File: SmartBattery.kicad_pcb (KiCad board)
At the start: 4 copper layers, 100 x 80 mm, 479 parts, among them J1 USB_C_Receptacle_USB2.0, J10 JST 2P-1.0, J11 JST 2P-1.0, J12 Conn_02x05_Odd_Even, J13 Conn_01x03_Male, J14 Conn_01x03_Male, J15 USB_C_Receptacle_USB2.0, J16 DM3AT-SF-PEJM5, J17 Conn_02x05_Odd_Even, J2 ST-USB-003A, J3 JACK-C-PC-10A-RA(R), J4 JST 2P-1.0, J5 JST 2P-1.0, J6 JST 2P-1.0, J7 JST 2P-1.0, J8 JST 2P-1.0, J9 JST 2P-1.0, Q1 VBA2625, Q10 AON7400A, Q11 AON7400A, Q12 BSC067N06LS3, Q13 BSC067N06LS3, Q14 2n7002K, Q15 VBA2625, Q16 VBA2625, Q17 VBA2625, Q18 VBA2625, Q19 VBA2625, Q2 2n7002K, Q20 LBSS84LT1G, Q21 2N7002, Q22 AO3401A, Q23 VBA2625, Q24 VBA2625, Q25 2n7002K, Q26 VBA2625, Q27 VBA2625, Q28 LBSS84LT1G, Q29 2N7002, Q3 AON7400A, Q30 2N7002, Q31 LBSS84LT1G, Q4 AON7400A, Q5 AON7400A, Q6 AON7400A, Q7 2n7002K, Q8 AON7400A, Q9 AON7400A, SW1 SW_Push, SW2 SW_Push, SW3 SW_Push, SW4 SW_Push, U1 BQ25703ARSNR, U10 ESP32-WROOM-32U, U11 STUSB4500, U12 STUSB4700, U13 TPS2511DGNR, U14 HT7533-1, U15 LMR14030SDDAR, U16 CH340G, U2 BQ294706DSGR, U3 ITV4030, U4 BQ40Z50, U5 LM5175PWPR, U6 STM32F730R8T6, U7 LY68L6400SLIT, U8 LMR14030SDDAR, U9 FS35ND01G-S1Y2QWFI000, Y1 Q13FC1350000400, Y2 24MHz, Y3 12MHz

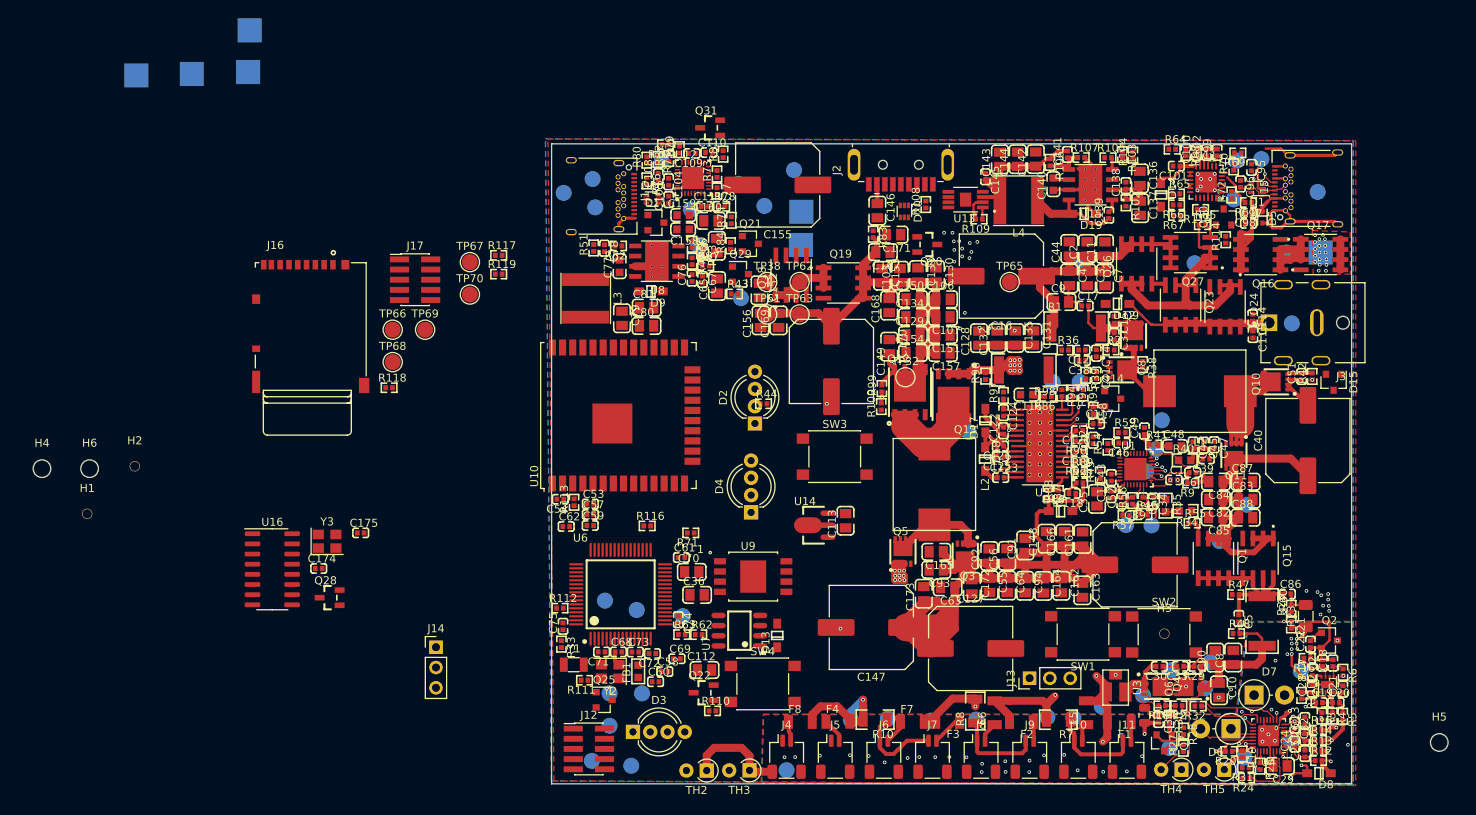
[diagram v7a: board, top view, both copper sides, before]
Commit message: Modified connections, added current limit
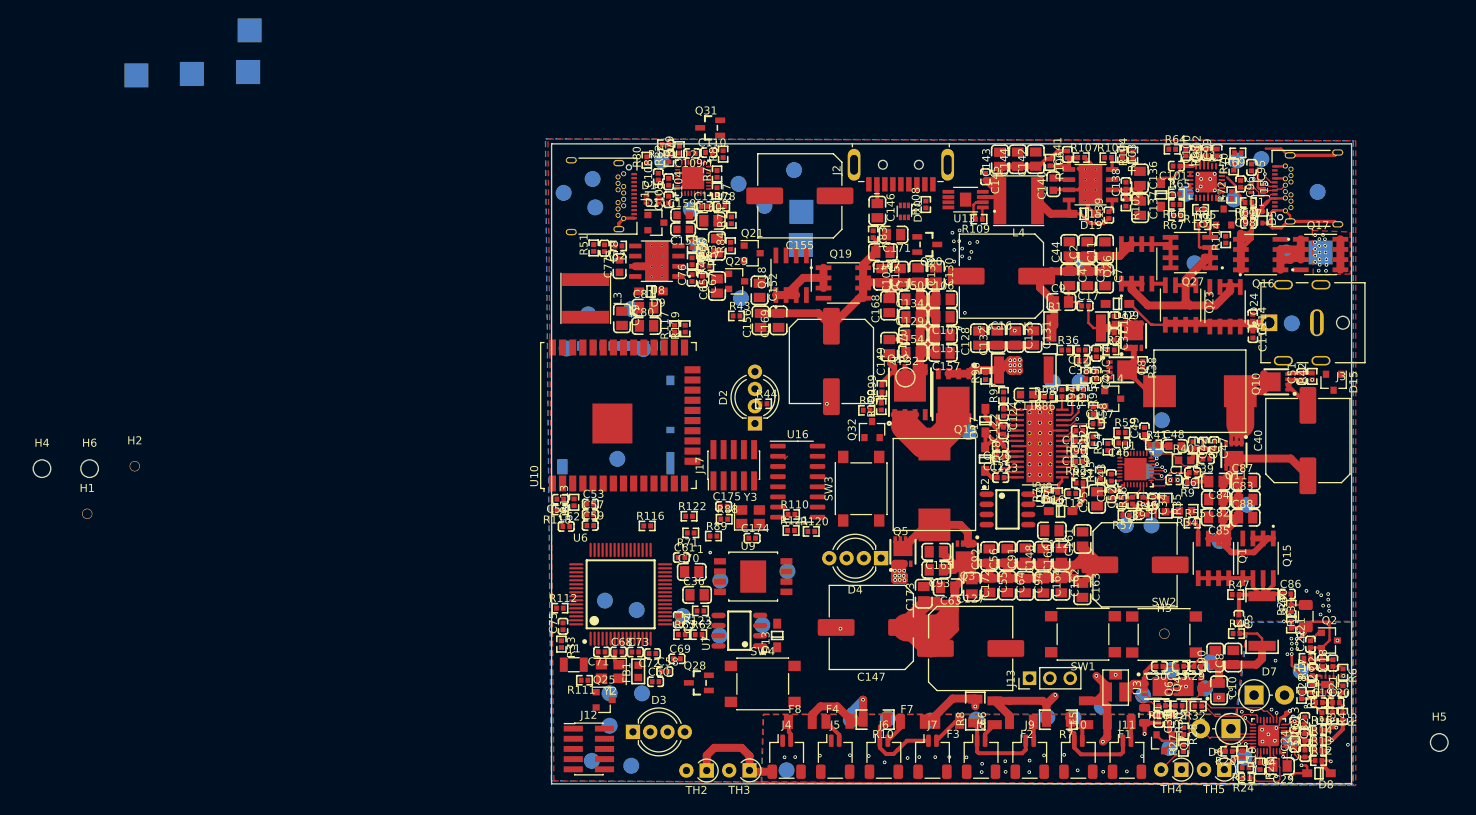
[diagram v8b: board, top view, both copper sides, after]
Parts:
- removed C113: 10u, lc_lib:0805_C
- removed J14: Conn_01x03_Male, Connector_PinHeader_2.54mm:PinHeader_1x03_P2.54mm_Vertical
- removed Q22: AO3401A, lc_lib:SOT-23(SOT-23-3)
- added Q32: 2N7002, Package_TO_SOT_SMD:SOT-23, F.Cu at (40.1, 35.7)
- added R120: 100k, lc_lib:0402_R, F.Cu at (32.5, 48.5)
- added R121: 100k, lc_lib:0402_R, F.Cu at (29.9, 48.3)
- added R122: 100k, lc_lib:0402_R, F.Cu at (17.2, 46.5)
- added R123: 50k, lc_lib:0402_R, F.Cu at (18.6, 58.4)
- C112: value 10u -> 2.2u 6.3v
- J16, TP38, TP61, TP62, TP63, TP65, TP66, TP67, TP68, TP69, TP70: moved to B.Cu
- Q31: value LBSS84LT1G -> AO3401A
- R100: value ?? -> 20k
- R88, R89: value ?? -> 100k
- R99: value ?? -> 280k
- U14: value HT7533-1 -> MCP6002-xMC; footprint lc_lib:SOT-89(SOT-89-3) -> lc_lib:SOIC-8_150MIL
- moved U16 66.6 mm to (30.8, 42.2)
- moved R76 64.7 mm to (63.3, 44.0), turned to 90 degrees
- moved R75 64.2 mm to (61.9, 43.9), turned to 90 degrees
- moved C174 54.3 mm to (25.1, 49.3)
- moved Y3 53.0 mm to (24.9, 46.6)
- moved Q28 47.4 mm to (18.4, 67.4)
- moved C112 46.8 mm to (62.5, 48.4), turned to 180 degrees
- moved R89 46.4 mm to (20.2, 49.0)
- moved J17 46.1 mm to (22.8, 40.2), turned to 90 degrees
- moved C175 45.5 mm to (21.5, 45.3)
- moved TP38 42.9 mm to (26.3, 60.2)
- moved R88 41.9 mm to (21.6, 46.9), turned to 0 degrees
- moved TP61 40.6 mm to (21.0, 61.5)
- moved J16 40.3 mm to (8.45, 25.3), turned to 180 degrees
- moved TP62 38.6 mm to (21.1, 54.6)
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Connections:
- net /Charger/ADAPTER_IN renamed /ADAPTER_IN
- net /OutputStage/VOLTAGE_CONTROL renamed Net-(R100-Pad2)
- C1 pad 1: /Charger/IBAT -> /IBAT
- C101 pad 1: /type_c_input/INPUT_TYPEC_VBUS_RAW -> /INPUT_TYPEC_RAW
- C103 pad 1: /Type_C_Output/OUTPUT_TYPEC_PWR -> /OUTPUT_VOLTAGE
- C106 pad 1: /Type_C_Output/OUTPUT_TYPEC_PWR -> /OUTPUT_VOLTAGE
- C107 pad 2: /Type_C_Output/OUTPUT_TYPEC_PWR -> /OUTPUT_VOLTAGE
- C112 pad 2: Net-(C112-Pad2) -> +3.3VP
- C114 pad 2: /Barrel_Jack_Input/BARREL_RAW -> /BARREL_RAW
- C115 pad 1: /Barrel_Jack_Input/BARREL_RAW -> /BARREL_RAW
- C128 pad 1: /Type_C_Output/OUTPUT_TYPEC_PWR -> /OUTPUT_VOLTAGE
- C129 pad 2: /Type_C_Output/OUTPUT_TYPEC_PWR -> /OUTPUT_VOLTAGE
- C130 pad 2: /Type_C_Output/OUTPUT_TYPEC_PWR -> /OUTPUT_VOLTAGE
- C131 pad 2: /Type_C_Output/OUTPUT_TYPEC_PWR -> /OUTPUT_VOLTAGE
- C132 pad 1: /Type_C_Output/OUTPUT_TYPEC_PWR -> /OUTPUT_VOLTAGE
- C133 pad 2: /Type_C_Output/OUTPUT_TYPEC_PWR -> /OUTPUT_VOLTAGE
- C134 pad 2: /Type_C_Output/OUTPUT_TYPEC_PWR -> /OUTPUT_VOLTAGE
- C135 pad 2: /Type_C_Output/OUTPUT_TYPEC_PWR -> /OUTPUT_VOLTAGE
- C149 pad 1: /Type_C_Output/OUTPUT_TYPEC_PWR -> /OUTPUT_VOLTAGE
- C150 pad 2: /Type_C_Output/OUTPUT_TYPEC_PWR -> /OUTPUT_VOLTAGE
- C151 pad 2: /Type_C_Output/OUTPUT_TYPEC_PWR -> /OUTPUT_VOLTAGE
- C152 pad 2: /Type_C_Output/OUTPUT_TYPEC_PWR -> /OUTPUT_VOLTAGE
- C153 pad 2: /Type_C_Output/OUTPUT_TYPEC_PWR -> /OUTPUT_VOLTAGE
- C154 pad 2: /Type_C_Output/OUTPUT_TYPEC_PWR -> /OUTPUT_VOLTAGE
- C155 pad 1: /Type_C_Output/OUTPUT_TYPEC_PWR -> /OUTPUT_VOLTAGE
- C156 pad 2: /Type_C_Output/OUTPUT_TYPEC_PWR -> /OUTPUT_VOLTAGE
- C157 pad 2: /Type_C_Output/OUTPUT_TYPEC_PWR -> /OUTPUT_VOLTAGE
- C167 pad 2: /Type_C_Output/OUTPUT_TYPEC_PWR -> /OUTPUT_VOLTAGE
- C168 pad 2: /Type_C_Output/OUTPUT_TYPEC_PWR -> /OUTPUT_VOLTAGE
- C169 pad 2: /Type_C_Output/OUTPUT_TYPEC_PWR -> /OUTPUT_VOLTAGE
- C170 pad 2: /Type_C_Output/OUTPUT_TYPEC_PWR -> /OUTPUT_VOLTAGE
- C171 pad 2: /Type_C_Output/OUTPUT_TYPEC_PWR -> /OUTPUT_VOLTAGE
- C34 pad 1: /Charger/IADP -> /IADP
- C6 pad 2: /Charger/PSYS -> /PSYS
- C78 pad 2: /Peripheral_3p3v/3p3v -> +3.3VP
- C79 pad 1: /Peripheral_3p3v/3p3v -> +3.3VP
- C80 pad 1: /Peripheral_3p3v/3p3v -> +3.3VP
- C81 pad 1: /Peripheral_3p3v/3p3v -> +3.3VP
- C97 pad 2: /type_c_input/INPUT_TYPEC_VBUS_RAW -> /INPUT_TYPEC_RAW
- C98 pad 1: /type_c_input/INPUT_TYPEC_VBUS_RAW -> /INPUT_TYPEC_RAW
- D12 pad 1: Net-(C112-Pad2) -> /BYPASS_VSYS
- D12 pad 2: /Barrel_Jack_Input/BARREL_RAW -> /BARREL_RAW
- D13 pad 1: +3.3VP -> /BYPASS_VSYS
- D13 pad 2: Net-(C113-Pad2) -> /Charger/VSYS
- D14 pad 1: Net-(C112-Pad2) -> /BYPASS_VSYS
- D14 pad 2: /type_c_input/INPUT_TYPEC_VBUS_RAW -> /INPUT_TYPEC_RAW
- D15 pad 1: /Barrel_Jack_Input/BARREL_RAW -> /BARREL_RAW
- D15 pad 2: /Barrel_Jack_Input/BARREL_RAW -> /BARREL_RAW
- D5 pad 2: /type_c_input/INPUT_TYPEC_VBUS_RAW -> /INPUT_TYPEC_RAW
- J13 pad 1: Net-(J13-Pad1) -> /BATT_SMB_D
- J13 pad 2: Net-(J13-Pad2) -> /BATT_SMB_C
- J13 pad 3: Net-(J13-Pad3) -> GND
- J15 pad A4: /type_c_input/INPUT_TYPEC_VBUS_RAW -> /INPUT_TYPEC_RAW
- J15 pad A9: /type_c_input/INPUT_TYPEC_VBUS_RAW -> /INPUT_TYPEC_RAW
- J15 pad B4: /type_c_input/INPUT_TYPEC_VBUS_RAW -> /INPUT_TYPEC_RAW
- J15 pad B9: /type_c_input/INPUT_TYPEC_VBUS_RAW -> /INPUT_TYPEC_RAW
- J3 pad 1: /Barrel_Jack_Input/BARREL_RAW -> /BARREL_RAW
- L3 pad 2: /Peripheral_3p3v/3p3v -> +3.3VP
- Q12 pad 0: /Type_C_Output/OUTPUT_TYPEC_PWR -> /OUTPUT_VOLTAGE
- Q12 pad 5: /Type_C_Output/OUTPUT_TYPEC_PWR -> /OUTPUT_VOLTAGE
- Q12 pad 6: /Type_C_Output/OUTPUT_TYPEC_PWR -> /OUTPUT_VOLTAGE
- Q12 pad 7: /Type_C_Output/OUTPUT_TYPEC_PWR -> /OUTPUT_VOLTAGE
- Q12 pad 8: /Type_C_Output/OUTPUT_TYPEC_PWR -> /OUTPUT_VOLTAGE
- Q16 pad 5: /type_c_input/INPUT_TYPEC_VBUS_RAW -> /INPUT_TYPEC_RAW
- Q16 pad 6: /type_c_input/INPUT_TYPEC_VBUS_RAW -> /INPUT_TYPEC_RAW
- Q16 pad 7: /type_c_input/INPUT_TYPEC_VBUS_RAW -> /INPUT_TYPEC_RAW
- Q16 pad 8: /type_c_input/INPUT_TYPEC_VBUS_RAW -> /INPUT_TYPEC_RAW
- Q19 pad 5: /Type_C_Output/OUTPUT_TYPEC_PWR -> /OUTPUT_VOLTAGE
- Q19 pad 6: /Type_C_Output/OUTPUT_TYPEC_PWR -> /OUTPUT_VOLTAGE
- Q19 pad 7: /Type_C_Output/OUTPUT_TYPEC_PWR -> /OUTPUT_VOLTAGE
- Q19 pad 8: /Type_C_Output/OUTPUT_TYPEC_PWR -> /OUTPUT_VOLTAGE
- Q20 pad 2: /Type_C_Output/OUTPUT_TYPEC_PWR -> /OUTPUT_VOLTAGE
- Q23 pad 5: /Barrel_Jack_Input/BARREL_RAW -> /BARREL_RAW
- Q23 pad 6: /Barrel_Jack_Input/BARREL_RAW -> /BARREL_RAW
- Q23 pad 7: /Barrel_Jack_Input/BARREL_RAW -> /BARREL_RAW
- Q23 pad 8: /Barrel_Jack_Input/BARREL_RAW -> /BARREL_RAW
- Q24 pad 5: /Barrel_Jack_Input/BARREL_RAW -> /BARREL_RAW
- Q24 pad 6: /Barrel_Jack_Input/BARREL_RAW -> /BARREL_RAW
- Q24 pad 7: /Barrel_Jack_Input/BARREL_RAW -> /BARREL_RAW
- Q24 pad 8: /Barrel_Jack_Input/BARREL_RAW -> /BARREL_RAW
- Q30 pad 3: /type_c_input/INPUT_TYPEC_VBUS_RAW -> /INPUT_TYPEC_RAW
- R102 pad 2: /Charger/VSYS -> /BYPASS_VSYS
- R110 pad 1: Net-(Q22-Pad1) -> /BARREL_RAW
- R110 pad 2: +3.3VP -> /MCU/ADC1_IN11
- R115 pad 2: /type_c_input/INPUT_TYPEC_VBUS_RAW -> /INPUT_TYPEC_RAW
- R35 pad 1: /Charger/IADP -> /IADP
- R37 pad 2: /Charger/VSYS -> /BYPASS_VSYS
- R51 pad 1: /Peripheral_3p3v/3p3v -> +3.3VP
- R61 pad 1: /type_c_input/INPUT_TYPEC_VBUS_RAW -> /INPUT_TYPEC_RAW
- R75 pad 1: /Type_C_Output/OUTPUT_TYPEC_VBUS_DIV7 -> GND
- R75 pad 2: GND -> /RESET_OVERCURRENT
- R76 pad 1: /Type_C_Output/OUTPUT_TYPEC_VBUS_DIV7 -> /OUTPUT_ENABLE
- R76 pad 2: Net-(C158-Pad2) -> /RESET_OVERCURRENT
- R83 pad 2: /Type_C_Output/OUTPUT_TYPEC_PWR -> /OUTPUT_VOLTAGE
- R87 pad 1: Net-(R87-Pad1) -> Net-(Q32-Pad3)
- R87 pad 2: /Charger/VSYS -> /OUTPUT_VOLTAGE
- R88 pad 1: GND -> /INPUT_TYPEC_RAW
- R88 pad 2: Net-(R87-Pad1) -> /MCU/ADC1_IN10
- R89 pad 1: Net-(R89-Pad1) -> /MCU/ADC1_IN10
- R89 pad 2: /Charger/VSYS -> GND
- R9 pad 2: /Charger/PSYS -> /PSYS
- R95 pad 1: /Type_C_Output/OUTPUT_TYPEC_PWR -> /OUTPUT_VOLTAGE
- R99 pad 2: /Type_C_Output/OUTPUT_TYPEC_PWR -> /OUTPUT_VOLTAGE
- TP31 pad 1: /type_c_input/INPUT_TYPEC_VBUS_RAW -> /INPUT_TYPEC_RAW
- TP44 pad 1: /Barrel_Jack_Input/BARREL_RAW -> /BARREL_RAW
- TP50 pad 1: /Type_C_Output/OUTPUT_TYPEC_PWR -> /OUTPUT_VOLTAGE
- TP55 pad 1: /Type_C_Output/OUTPUT_TYPEC_PWR -> /OUTPUT_VOLTAGE
- U1 pad 10: /Charger/PSYS -> /PSYS
- U1 pad 8: /Charger/IADP -> /IADP
- U1 pad 9: /Charger/IBAT -> /IBAT
- U11 pad 24: /type_c_input/INPUT_TYPEC_VBUS_RAW -> /INPUT_TYPEC_RAW
- U14 pad 1: GND -> /CURRENT_TRIP
- U14 pad 2: Net-(C112-Pad2) -> /PSYS
- U14 pad 3: Net-(C113-Pad2) -> /DAC1
- U5 pad 1: Net-(R87-Pad1) -> /OUTPUT_ENABLE
- U5 pad 12: /Type_C_Output/OUTPUT_TYPEC_PWR -> /OUTPUT_VOLTAGE
- U5 pad 3: Net-(R89-Pad1) -> /Charger/VSYS
- U6 pad 11: /MCU/ADC1_IN13 -> /IADP
- U6 pad 20: /MCU/DAC1 -> /DAC1
- U6 pad 21: /MCU/DAC2 -> /DAC2
- U6 pad 24: /MCU/ADC1_IN14 -> /IBAT
- U6 pad 26: Net-(U6-Pad26) -> /PSYS
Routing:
- net /Barrel_Jack_Input/BARREL_RAW: track 38.2 -> 0.00 mm
- net /BARREL_RAW: track 0.00 -> 38.2 mm
- net /type_c_input/INPUT_TYPEC_VBUS_RAW: track 34.7 -> 0.00 mm
- net /INPUT_TYPEC_RAW: track 0.00 -> 34.7 mm
- net /Type_C_Output/OUTPUT_TYPEC_PWR: track 128.0 -> 94.7 mm, vias 1 -> 0
- net /OUTPUT_VOLTAGE: track 0.00 -> 33.2 mm, vias 0 -> 1
- net /Charger/VSYS: track 194.3 -> 168.3 mm
- net /PSYS: track 0.00 -> 7.04 mm
- net /Charger/PSYS: track 7.04 -> 0.00 mm
- net GND: track 109.8 -> 106.6 mm
- net /IBAT: track 0.00 -> 3.16 mm, vias 0 -> 1
- net /Charger/IBAT: track 3.16 -> 0.00 mm, vias 1 -> 0
- net Net-(R87-Pad1): track 3.14 -> 0.00 mm
- net /OUTPUT_ENABLE: track 0.00 -> 3.14 mm
- net Net-(R89-Pad1): track 2.00 -> 0.00 mm
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- added copper zone on F.Cu, net /Charger/ADAPTER_IN
- added copper zone on In2.Cu, net /Charger/ADAPTER_IN
- removed copper zone on F.Cu, net /ADAPTER_IN
- removed copper zone on In2.Cu, net /ADAPTER_IN
